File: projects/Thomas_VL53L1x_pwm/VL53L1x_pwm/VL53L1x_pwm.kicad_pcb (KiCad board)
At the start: 2 copper layers, 33 x 26 mm, 31 parts, among them J1 Conn_02x05_Odd_Even, J2 Conn_01x04, Q1 BSS138, Q2 BSS138, Q3 BSS138, Q4 BSS138, U1 LP2985-1.8, U2 STM32L011D4Px, U3 VL53L1CXV0FY1, Y1 16 MHz 9 pF

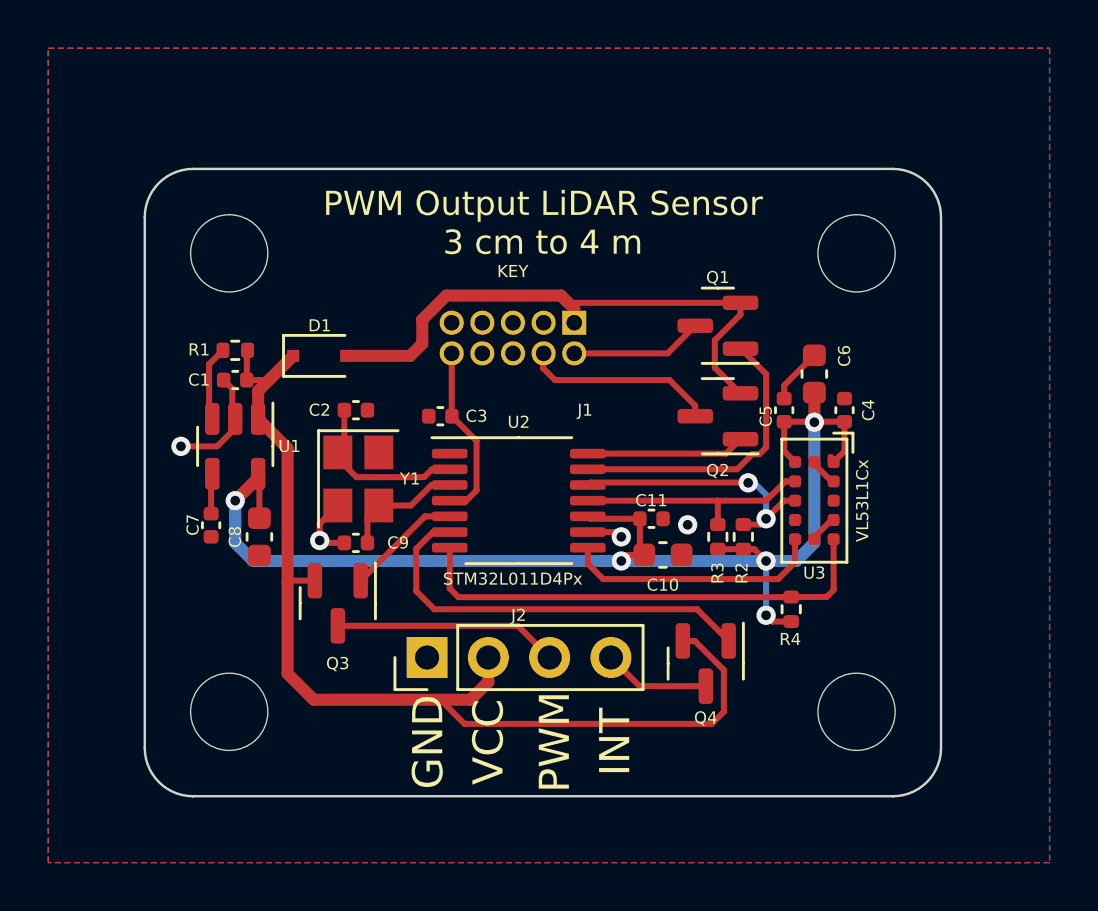
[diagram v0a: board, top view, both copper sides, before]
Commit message: Fix really stupid hardware bug Lesson learned: check spice BEFORE committing
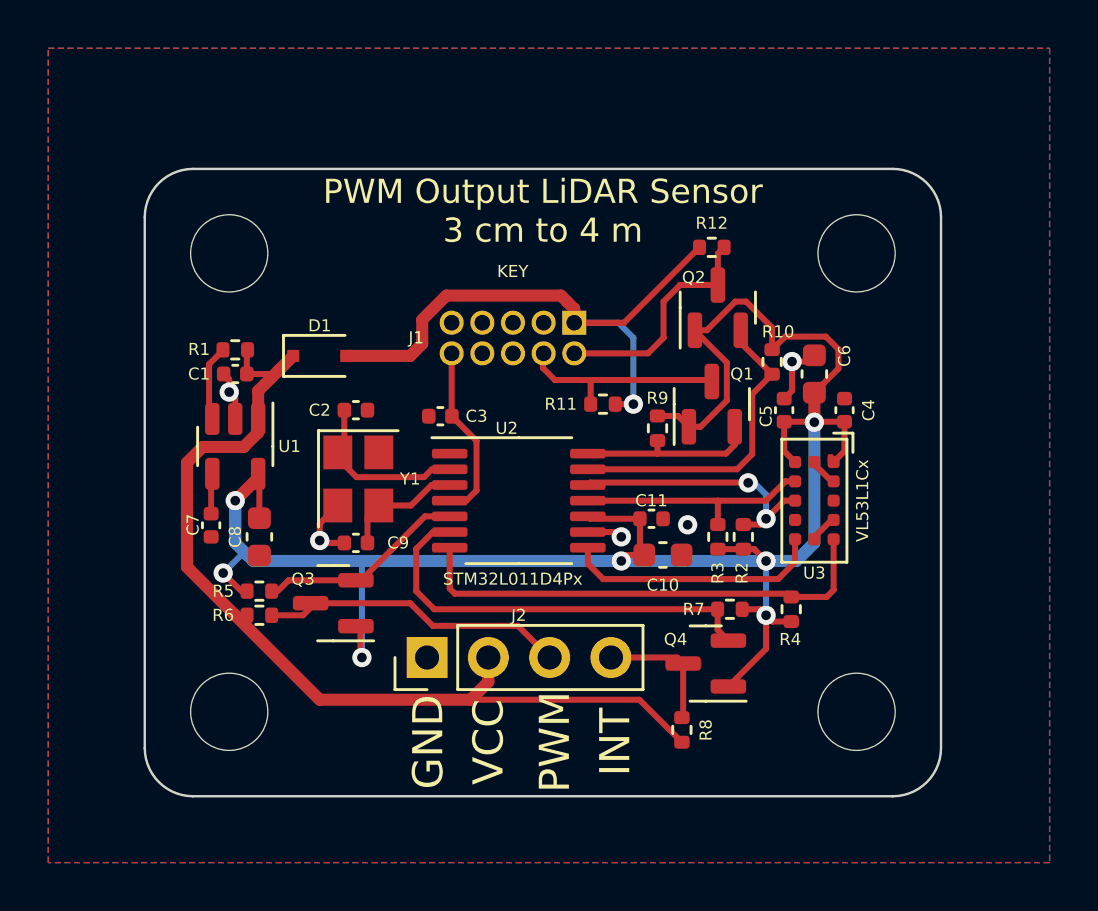
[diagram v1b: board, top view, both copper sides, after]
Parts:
- added R10: 10k, Resistor_SMD:R_0402_1005Metric, F.Cu at (143.5, 94.0)
- added R11: 10k, Resistor_SMD:R_0402_1005Metric, F.Cu at (136.5, 95.8)
- added R12: 10k, Resistor_SMD:R_0402_1005Metric, F.Cu at (141.0, 89.2)
- added R5: 10k, Resistor_SMD:R_0402_1005Metric, F.Cu at (122.2, 103.5)
- added R6: 10k, Resistor_SMD:R_0402_1005Metric, F.Cu at (122.2, 104.5)
- added R7: 10k, Resistor_SMD:R_0402_1005Metric, F.Cu at (141.8, 104.2)
- added R8: 10k, Resistor_SMD:R_0402_1005Metric, F.Cu at (139.8, 109.2)
- added R9: 10k, Resistor_SMD:R_0402_1005Metric, F.Cu at (138.8, 96.8)
- moved Q2 4.50 mm to (141.2, 91.8), turned to 90 degrees
- moved Q1 3.26 mm to (141.0, 95.8), turned to 90 degrees
- moved C1 0.25 mm to (121.2, 94.5)
- moved Q3 0.19 mm to (125.3, 104.0), turned to 180 degrees
- turned Q4 to 180 degrees
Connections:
- Q1 pad 1: SWDIO1V8 -> +1V8
- Q1 pad 2: +3V3 -> SWCLK1V8
- Q1 pad 3: SWDIO -> SWCLK
- Q2 pad 1: SWCLK1V8 -> +1V8
- Q2 pad 2: +3V3 -> SWDIO1V8
- Q2 pad 3: SWCLK -> SWDIO
- Q3 pad 1: PWMOUT1V8 -> +1V8
- Q3 pad 2: VCC -> PWMOUT1V8
- Q4 pad 1: INTOUT1V8 -> +1V8
- Q4 pad 2: VCC -> INTOUT1V8
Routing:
- net +1V8: track 52.1 -> 81.9 mm, vias 5 -> 7
- net VCC: track 43.9 -> 39.5 mm
- net SWDIO: track 5.49 -> 9.67 mm
- net PWMOUT1V8: track 4.79 -> 8.40 mm
- net PWMOUT: track 9.32 -> 12.4 mm
- net GND: track 12.8 -> 10.7 mm, vias 4 -> 5
- net SWCLK1V8: track 6.57 -> 7.53 mm
- net +3V3: track 23.7 -> 24.6 mm, vias 0 -> 1
- net INTOUT: track 4.42 -> 5.28 mm
- net SWCLK: track 8.01 -> 8.73 mm
